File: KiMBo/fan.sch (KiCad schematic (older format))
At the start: 36 parts, among them Q14 2N7002, Q15 DMP3098L-7, Q16 2N7002, Q17 DMP3098L-7, Q18 2N7002, Q19 DMP3098L-7

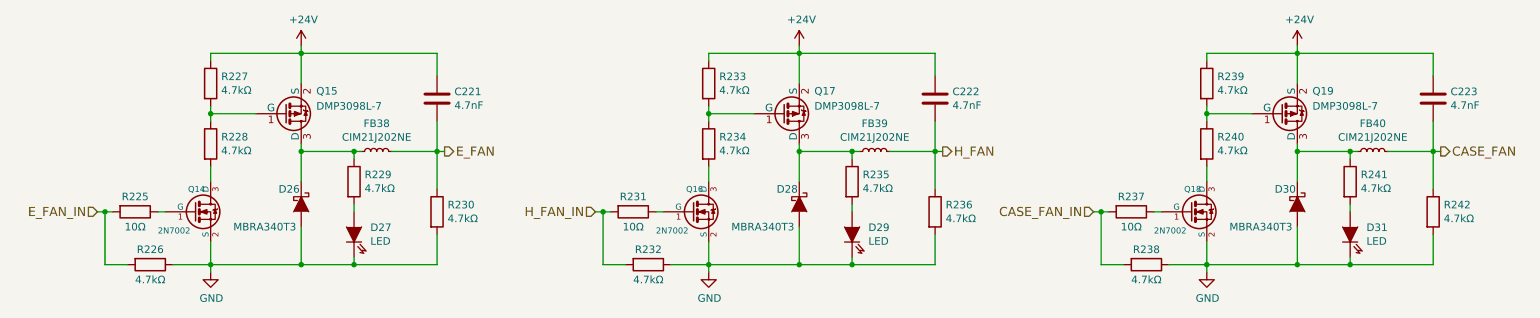
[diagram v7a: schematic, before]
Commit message: Connect X and Z stepper driver open-drain DIAG0 and DIAG1 lines together
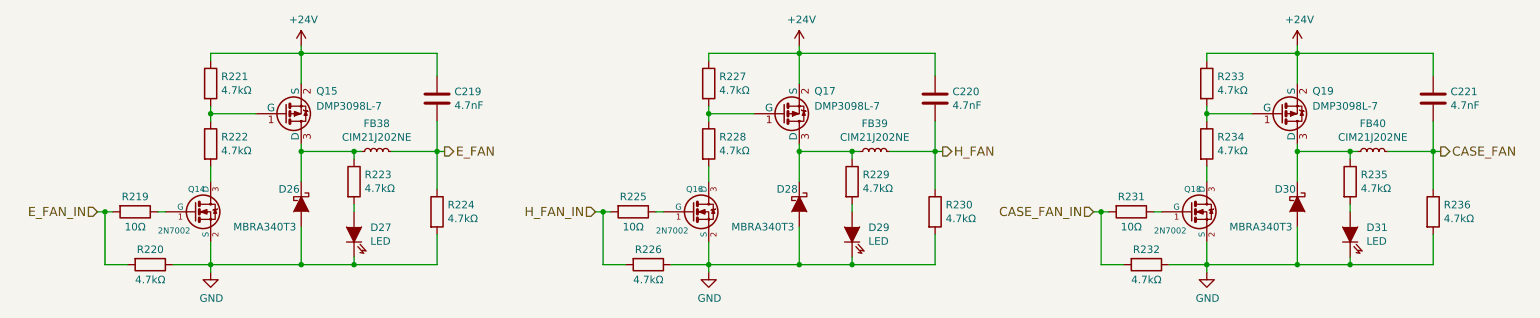
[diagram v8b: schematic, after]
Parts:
- renumbered C221 to C219, C222 to C220, C223 to C221, R225 to R219, R226 to R220, R227 to R221, R228 to R222, R229 to R223, R230 to R224, R231 to R225, R232 to R226, R233 to R227, R234 to R228, R235 to R229, R236 to R230, R237 to R231, R238 to R232, R239 to R233, R240 to R234, R241 to R235, R242 to R236
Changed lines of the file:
@@
 E_FAN
 $Comp
-L +24V #PWR0288
+L +24V #PWR0278
 U 1 1 5B5EFE55
 P 4800 4500
-F 0 "#PWR0288" H 4800 4350 50  0001 C CNN
+F 0 "#PWR0278" H 4800 4350 50  0001 C CNN
 F 1 "+24V" H 4815 4673 50  0000 C CNN
 F 2 "" H 4800 4500 50  0000 C CNN
@@
 $EndComp
 $Comp
-L GND #PWR0289
+L GND #PWR0279
 U 1 1 5B5EFE5B
 P 4200 6000
-F 0 "#PWR0289" H 4200 5750 50  0001 C CNN
+F 0 "#PWR0279" H 4200 5750 50  0001 C CNN
 F 1 "GND" H 4205 5827 50  0000 C CNN
 F 2 "" H 4200 6000 50  0000 C CNN
@@
 $EndComp
 $Comp
-L R R225
+L R R219
 U 1 1 5B5EFE68
 P 3700 5600
-F 0 "R225" V 3600 5600 50  0000 C CNN
+F 0 "R219" V 3600 5600 50  0000 C CNN
 F 1 "10Ω" V 3800 5600 50  0000 C CNN
 F 2 "" V 3630 5600 50  0001 C CNN
@@
 $EndComp
 $Comp
-L R R229
+L R R223
 U 1 1 5B5EFE7E
 P 5150 5400
-F 0 "R229" H 5220 5446 50  0000 L CNN
+F 0 "R223" H 5220 5446 50  0000 L CNN
 F 1 "4.7kΩ" H 5220 5355 50  0000 L CNN
 F 2 "" V 5080 5400 50  0001 C CNN
@@
 $EndComp
 $Comp
-L R R227
+L R R221
 U 1 1 5B5EFE85
 P 4200 4750
-F 0 "R227" H 4270 4796 50  0000 L CNN
+F 0 "R221" H 4270 4796 50  0000 L CNN
 F 1 "4.7kΩ" H 4270 4705 50  0000 L CNN
 F 2 "" V 4130 4750 50  0001 C CNN
@@
 $EndComp
 $Comp
-L R R228
+L R R222
 U 1 1 5B5EFE8C
 P 4200 5150
-F 0 "R228" H 4270 5196 50  0000 L CNN
+F 0 "R222" H 4270 5196 50  0000 L CNN
 F 1 "4.7kΩ" H 4270 5105 50  0000 L CNN
 F 2 "" V 4130 5150 50  0001 C CNN
@@
 $EndComp
 $Comp
-L R R226
+L R R220
 U 1 1 5B5EFE93
 P 3800 5950
-F 0 "R226" V 3700 5950 50  0000 C CNN
+F 0 "R220" V 3700 5950 50  0000 C CNN
 F 1 "4.7kΩ" V 3900 5950 50  0000 C CNN
 F 2 "" V 3730 5950 50  0001 C CNN
@@
 $EndComp
 $Comp
-L R R230
+L R R224
 U 1 1 5B5EFE9A
 P 5700 5600
-F 0 "R230" H 5770 5646 50  0000 L CNN
+F 0 "R224" H 5770 5646 50  0000 L CNN
 F 1 "4.7kΩ" H 5770 5555 50  0000 L CNN
 F 2 "" V 5630 5600 50  0001 C CNN
@@
 $EndComp
 $Comp
-L C C221
+L C C219
 U 1 1 5B5EFEA1
 P 5700 4850
-F 0 "C221" H 5815 4896 50  0000 L CNN
+F 0 "C219" H 5815 4896 50  0000 L CNN
 F 1 "4.7nF" H 5815 4805 50  0000 L CNN
 F 2 "Capacitors_SMD:C_0402" H 5738 4700 50  0001 C CNN
@@
 H_FAN
 $Comp
-L +24V #PWR0290
+L +24V #PWR0280
 U 1 1 5B5F23AA
 P 8100 4500
-F 0 "#PWR0290" H 8100 4350 50  0001 C CNN
+F 0 "#PWR0280" H 8100 4350 50  0001 C CNN
 F 1 "+24V" H 8115 4673 50  0000 C CNN
 F 2 "" H 8100 4500 50  0000 C CNN
@@
 $EndComp
 $Comp
-L GND #PWR0291
+L GND #PWR0281
 U 1 1 5B5F23B0
 P 7500 6000
-F 0 "#PWR0291" H 7500 5750 50  0001 C CNN
+F 0 "#PWR0281" H 7500 5750 50  0001 C CNN
 F 1 "GND" H 7505 5827 50  0000 C CNN
 F 2 "" H 7500 6000 50  0000 C CNN
@@
 $EndComp
 $Comp
-L R R231
+L R R225
 U 1 1 5B5F23BD
 P 7000 5600
-F 0 "R231" V 6900 5600 50  0000 C CNN
+F 0 "R225" V 6900 5600 50  0000 C CNN
 F 1 "10Ω" V 7100 5600 50  0000 C CNN
 F 2 "" V 6930 5600 50  0001 C CNN
@@
 $EndComp
 $Comp
-L R R235
+L R R229
 U 1 1 5B5F23D2
 P 8450 5400
-F 0 "R235" H 8520 5446 50  0000 L CNN
+F 0 "R229" H 8520 5446 50  0000 L CNN
 F 1 "4.7kΩ" H 8520 5355 50  0000 L CNN
 F 2 "" V 8380 5400 50  0001 C CNN
@@
 $EndComp
 $Comp
-L R R233
+L R R227
 U 1 1 5B5F23D9
 P 7500 4750
-F 0 "R233" H 7570 4796 50  0000 L CNN
+F 0 "R227" H 7570 4796 50  0000 L CNN
 F 1 "4.7kΩ" H 7570 4705 50  0000 L CNN
 F 2 "" V 7430 4750 50  0001 C CNN
@@
 $EndComp
 $Comp
-L R R234
+L R R228
 U 1 1 5B5F23E0
 P 7500 5150
-F 0 "R234" H 7570 5196 50  0000 L CNN
+F 0 "R228" H 7570 5196 50  0000 L CNN
 F 1 "4.7kΩ" H 7570 5105 50  0000 L CNN
 F 2 "" V 7430 5150 50  0001 C CNN
@@
 $EndComp
 $Comp
-L R R232
+L R R226
 U 1 1 5B5F23E7
 P 7100 5950
-F 0 "R232" V 7000 5950 50  0000 C CNN
+F 0 "R226" V 7000 5950 50  0000 C CNN
 F 1 "4.7kΩ" V 7200 5950 50  0000 C CNN
 F 2 "" V 7030 5950 50  0001 C CNN
@@
 $EndComp
 $Comp
-L R R236
+L R R230
 U 1 1 5B5F23EE
 P 9000 5600
-F 0 "R236" H 9070 5646 50  0000 L CNN
+F 0 "R230" H 9070 5646 50  0000 L CNN
 F 1 "4.7kΩ" H 9070 5555 50  0000 L CNN
 F 2 "" V 8930 5600 50  0001 C CNN
@@
 $EndComp
 $Comp
-L C C222
+L C C220
 U 1 1 5B5F23F5
 P 9000 4850
-F 0 "C222" H 9115 4896 50  0000 L CNN
+F 0 "C220" H 9115 4896 50  0000 L CNN
 F 1 "4.7nF" H 9115 4805 50  0000 L CNN
 F 2 "Capacitors_SMD:C_0402" H 9038 4700 50  0001 C CNN
@@
 CASE_FAN
 $Comp
-L +24V #PWR0292
+L +24V #PWR0282
 U 1 1 5B5F2995
 P 11400 4500
-F 0 "#PWR0292" H 11400 4350 50  0001 C CNN
+F 0 "#PWR0282" H 11400 4350 50  0001 C CNN
 F 1 "+24V" H 11415 4673 50  0000 C CNN
 F 2 "" H 11400 4500 50  0000 C CNN
@@
 $EndComp
 $Comp
-L GND #PWR0293
+L GND #PWR0283
 U 1 1 5B5F299B
 P 10800 6000
-F 0 "#PWR0293" H 10800 5750 50  0001 C CNN
+F 0 "#PWR0283" H 10800 5750 50  0001 C CNN
 F 1 "GND" H 10805 5827 50  0000 C CNN
 F 2 "" H 10800 6000 50  0000 C CNN
@@
 $EndComp
 $Comp
-L R R237
+L R R231
 U 1 1 5B5F29A8
 P 10300 5600
-F 0 "R237" V 10200 5600 50  0000 C CNN
+F 0 "R231" V 10200 5600 50  0000 C CNN
 F 1 "10Ω" V 10400 5600 50  0000 C CNN
 F 2 "" V 10230 5600 50  0001 C CNN
@@
 $EndComp
 $Comp
-L R R241
+L R R235
 U 1 1 5B5F29BD
 P 11750 5400
-F 0 "R241" H 11820 5446 50  0000 L CNN
+F 0 "R235" H 11820 5446 50  0000 L CNN
 F 1 "4.7kΩ" H 11820 5355 50  0000 L CNN
 F 2 "" V 11680 5400 50  0001 C CNN
@@
 $EndComp
 $Comp
-L R R239
+L R R233
 U 1 1 5B5F29C4
 P 10800 4750
-F 0 "R239" H 10870 4796 50  0000 L CNN
+F 0 "R233" H 10870 4796 50  0000 L CNN
 F 1 "4.7kΩ" H 10870 4705 50  0000 L CNN
 F 2 "" V 10730 4750 50  0001 C CNN
@@
 $EndComp
 $Comp
-L R R240
+L R R234
 U 1 1 5B5F29CB
 P 10800 5150
-F 0 "R240" H 10870 5196 50  0000 L CNN
+F 0 "R234" H 10870 5196 50  0000 L CNN
 F 1 "4.7kΩ" H 10870 5105 50  0000 L CNN
 F 2 "" V 10730 5150 50  0001 C CNN
@@
 $EndComp
 $Comp
-L R R238
+L R R232
 U 1 1 5B5F29D2
 P 10400 5950
-F 0 "R238" V 10300 5950 50  0000 C CNN
+F 0 "R232" V 10300 5950 50  0000 C CNN
 F 1 "4.7kΩ" V 10500 5950 50  0000 C CNN
 F 2 "" V 10330 5950 50  0001 C CNN
@@
 $EndComp
 $Comp
-L R R242
+L R R236
 U 1 1 5B5F29D9
 P 12300 5600
-F 0 "R242" H 12370 5646 50  0000 L CNN
+F 0 "R236" H 12370 5646 50  0000 L CNN
 F 1 "4.7kΩ" H 12370 5555 50  0000 L CNN
 F 2 "" V 12230 5600 50  0001 C CNN
@@
 $EndComp
 $Comp
-L C C223
+L C C221
 U 1 1 5B5F29E0
 P 12300 4850
-F 0 "C223" H 12415 4896 50  0000 L CNN
+F 0 "C221" H 12415 4896 50  0000 L CNN
 F 1 "4.7nF" H 12415 4805 50  0000 L CNN
 F 2 "Capacitors_SMD:C_0402" H 12338 4700 50  0001 C CNN
